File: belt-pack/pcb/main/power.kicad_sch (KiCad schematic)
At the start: 6 parts, among them U2 TP4056

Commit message: Nearly finished with battery circuitry
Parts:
- added C1: 100nF, PCM_JLCPCB:C_0402, symbol PCM_JLCPCB-Capacitors:0402,100nF
- added C2, C3: 10uF, PCM_JLCPCB:C_0603, symbol PCM_JLCPCB-Capacitors:0603,10uF
- added D1: Red, PCM_JLCPCB:D_0603, symbol PCM_JLCPCB-Diodes:LED,0603,Red
- added D2: Green, PCM_JLCPCB:D_0805, symbol PCM_JLCPCB-Diodes:LED,0805,Green
- added R3: 100Ω, PCM_JLCPCB:R_0402, symbol PCM_JLCPCB-Resistors:0402,100Ω
- added R4, R5: 1kΩ, PCM_JLCPCB:R_0402, symbol PCM_JLCPCB-Resistors:0402,1kΩ
- added R6: 1Ω, PCM_JLCPCB:R_1206, symbol PCM_JLCPCB-Resistors:1206,1Ω
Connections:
- net GND: now also R2.2, C2.2, C3.2; no longer U2.6 (STDBY#), U2.7 (CHRG#)
- net USB_5V: now also R6.1; no longer U2.4 (VCC), U2.8 (CE)
- net at BT1.2 (-), Q1.1 (S1): now also C1.2
- net at Q1.6 (G1): now also U3.3 (OC)
- net at U2.5 (BAT): now also BT1.1 (+), C2.1, R3.1; no longer U3.5 (VCC)
- new net: C3.1, R4.1, R5.1, R6.2, U2.4 (VCC), U2.8 (CE)
- new net: D2.2, R5.2
- new net: C1.1, R3.2, U3.5 (VCC)
- new net: D1.2, R4.2
- new net: D2.1, U2.6 (STDBY#)
- new net: D1.1, U2.7 (CHRG#)
- no-connect marks 0 -> 1
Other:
- moved on the sheet: BT1, Q1, R1, R2, U2, U3

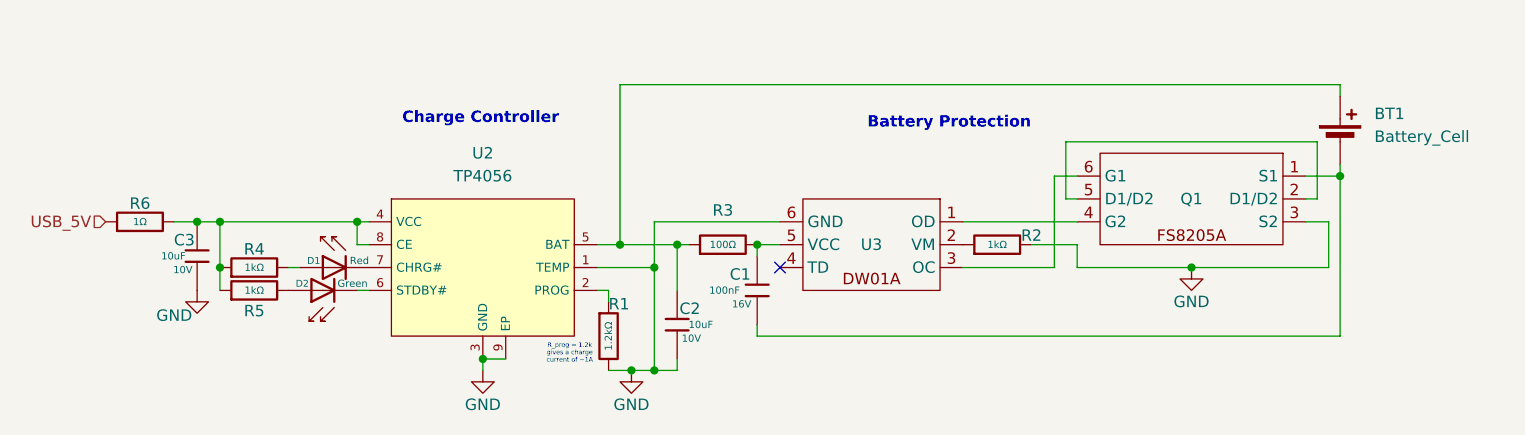
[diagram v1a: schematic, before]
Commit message: Schematic progress
battery charge circuit
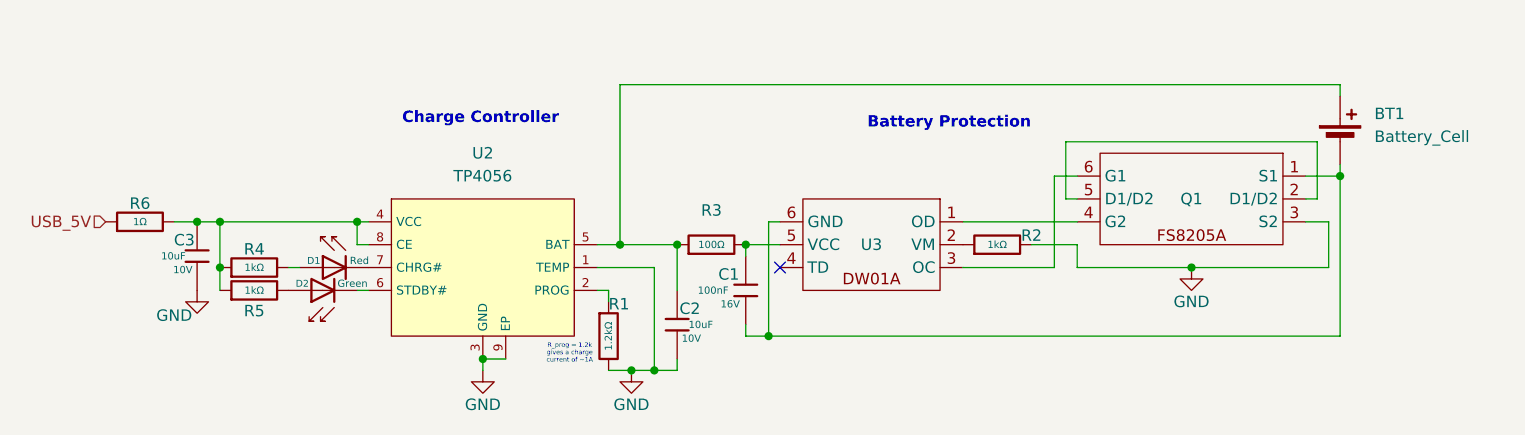
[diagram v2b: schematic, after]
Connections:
- net GND: no longer U3.6 (GND)
- net at BT1.2 (-), C1.2, Q1.1 (S1): now also U3.6 (GND)
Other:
- moved on the sheet: C1, R3
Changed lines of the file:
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@@
 	)
 	(junction
-		(at 165.1 118.11)
+		(at 156.21 118.11)
 		(diameter 0)
 		(color 0 0 0 0)
@@
 	)
 	(junction
-		(at 156.21 118.11)
-		(diameter 0)
-		(color 0 0 0 0)
-	)
-	(junction
-		(at 153.67 120.65)
+		(at 166.37 128.27)
 		(diameter 0)
 		(color 0 0 0 0)
@@
 	)
 	(junction
+		(at 163.83 118.11)
+		(diameter 0)
+		(color 0 0 0 0)
+	)
+	(junction
 		(at 120.65 115.57)
 		(diameter 0)
@@
 	(wire
 		(pts
+			(xy 166.37 115.57) (xy 166.37 128.27)
+		)
+		(stroke
+			(width 0)
+			(type default)
+		)
+	)
+	(wire
+		(pts
 			(xy 213.36 120.65) (xy 228.6 120.65)
 		)
@@
 	(wire
 		(pts
-			(xy 149.86 118.11) (xy 156.21 118.11)
+			(xy 166.37 128.27) (xy 229.87 128.27)
 		)
 		(stroke
@@
 	(wire
 		(pts
-			(xy 156.21 118.11) (xy 157.48 118.11)
+			(xy 149.86 118.11) (xy 156.21 118.11)
 		)
 		(stroke
@@
 	(wire
 		(pts
-			(xy 167.64 115.57) (xy 153.67 115.57)
+			(xy 227.33 106.68) (xy 199.39 106.68)
 		)
 		(stroke
@@
 	(wire
 		(pts
-			(xy 227.33 106.68) (xy 199.39 106.68)
+			(xy 167.64 115.57) (xy 166.37 115.57)
 		)
 		(stroke
@@
 	(wire
 		(pts
-			(xy 165.1 119.38) (xy 165.1 118.11)
+			(xy 163.83 119.38) (xy 163.83 118.11)
 		)
 		(stroke
@@
 	(wire
 		(pts
-			(xy 199.39 113.03) (xy 200.66 113.03)
+			(xy 163.83 118.11) (xy 167.64 118.11)
 		)
 		(stroke
@@
 	(wire
 		(pts
-			(xy 147.32 120.65) (xy 153.67 120.65)
+			(xy 199.39 113.03) (xy 200.66 113.03)
 		)
 		(stroke
@@
 	(wire
 		(pts
-			(xy 120.65 123.19) (xy 121.92 123.19)
+			(xy 147.32 120.65) (xy 153.67 120.65)
 		)
 		(stroke
@@
 	(wire
 		(pts
-			(xy 147.32 118.11) (xy 149.86 118.11)
+			(xy 120.65 123.19) (xy 121.92 123.19)
 		)
 		(stroke
@@
 	(wire
 		(pts
-			(xy 165.1 128.27) (xy 229.87 128.27)
+			(xy 147.32 118.11) (xy 149.86 118.11)
 		)
 		(stroke
@@
 	(wire
 		(pts
-			(xy 229.87 100.33) (xy 149.86 100.33)
+			(xy 163.83 128.27) (xy 166.37 128.27)
 		)
 		(stroke
@@
 	(wire
 		(pts
-			(xy 187.96 120.65) (xy 198.12 120.65)
+			(xy 229.87 100.33) (xy 149.86 100.33)
 		)
 		(stroke
@@
 	(wire
 		(pts
-			(xy 199.39 106.68) (xy 199.39 113.03)
+			(xy 187.96 120.65) (xy 198.12 120.65)
 		)
 		(stroke
@@
 	(wire
 		(pts
-			(xy 153.67 115.57) (xy 153.67 120.65)
+			(xy 199.39 106.68) (xy 199.39 113.03)
 		)
 		(stroke
@@
 	(wire
 		(pts
-			(xy 165.1 128.27) (xy 165.1 127)
+			(xy 163.83 128.27) (xy 163.83 127)
 		)
 		(stroke
@@
 	(wire
 		(pts
-			(xy 165.1 118.11) (xy 167.64 118.11)
-		)
-		(stroke
-			(width 0)
-			(type default)
-		)
-	)
-	(wire
-		(pts
 			(xy 102.87 115.57) (xy 105.41 115.57)
 		)
@@
 	(symbol
 		(lib_id "PCM_JLCPCB-Resistors:0402,100Ω")
-		(at 161.29 118.11 90)
+		(at 160.02 118.11 90)
 		(unit 1)
 		(body_style 1)
@@
 		(fields_autoplaced yes)
 		(property "Reference" "R3"
-			(at 161.29 114.3 90)
+			(at 160.02 114.3 90)
 			(show_name no)
 			(do_not_autoplace no)
@@
 		)
 		(property "Value" "100Ω"
-			(at 161.29 118.11 90)
+			(at 160.02 118.11 90)
 			(show_name no)
 			(do_not_autoplace yes)
@@
 		)
 		(property "Footprint" "PCM_JLCPCB:R_0402"
-			(at 161.29 119.888 90)
+			(at 160.02 119.888 90)
 			(hide yes)
 			(show_name no)
@@
 		)
 		(property "Datasheet" "https://www.lcsc.com/datasheet/lcsc_datasheet_2205311900_UNI-ROYAL-Uniroyal-Elec-0402WGF1000TCE_C25076.pdf"
-			(at 161.29 118.11 0)
+			(at 160.02 118.11 0)
 			(hide yes)
 			(show_name no)
@@
 		)
 		(property "Description" "62.5mW Thick Film Resistors 50V ±1% ±200ppm/°C 100Ω 0402 Chip Resistor - Surface Mount ROHS"
-			(at 161.29 118.11 0)
+			(at 160.02 118.11 0)
 			(hide yes)
 			(show_name no)
@@
 		)
 		(property "LCSC" "C25076"
-			(at 161.29 118.11 0)
+			(at 160.02 118.11 0)
 			(hide yes)
 			(show_name no)
@@
 		)
 		(property "Stock" "5907585"
-			(at 161.29 118.11 0)
+			(at 160.02 118.11 0)
 			(hide yes)
 			(show_name no)
@@
 		)
 		(property "Price" "0.004USD"
-			(at 161.29 118.11 0)
+			(at 160.02 118.11 0)
 			(hide yes)
 			(show_name no)
@@
 		)
 		(property "Process" "SMT"
-			(at 161.29 118.11 0)
+			(at 160.02 118.11 0)
 			(hide yes)
 			(show_name no)
@@
 		)
 		(property "Minimum Qty" "20"
-			(at 161.29 118.11 0)
+			(at 160.02 118.11 0)
 			(hide yes)
 			(show_name no)
@@
 		)
 		(property "Attrition Qty" "10"
-			(at 161.29 118.11 0)
+			(at 160.02 118.11 0)
 			(hide yes)
 			(show_name no)
@@
 		)
 		(property "Class" "Basic Component"
-			(at 161.29 118.11 0)
+			(at 160.02 118.11 0)
 			(hide yes)
 			(show_name no)
@@
 		)
 		(property "Category" "Resistors,Chip Resistor - Surface Mount"
-			(at 161.29 118.11 0)
+			(at 160.02 118.11 0)
 			(hide yes)
 			(show_name no)
@@
 		)
 		(property "Manufacturer" "UNI-ROYAL(Uniroyal Elec)"
-			(at 161.29 118.11 0)
+			(at 160.02 118.11 0)
 			(hide yes)
 			(show_name no)
@@
 		)
 		(property "Part" "0402WGF1000TCE"
-			(at 161.29 118.11 0)
+			(at 160.02 118.11 0)
 			(hide yes)
 			(show_name no)
@@
 		)
 		(property "Resistance" "100Ω"
-			(at 161.29 118.11 0)
+			(at 160.02 118.11 0)
 			(hide yes)
 			(show_name no)
@@
 		)
 		(property "Power(Watts)" "62.5mW"
-			(at 161.29 118.11 0)
+			(at 160.02 118.11 0)
 			(hide yes)
 			(show_name no)
@@
 		)
 		(property "Type" "Thick Film Resistors"
-			(at 161.29 118.11 0)
+			(at 160.02 118.11 0)
 			(hide yes)
 			(show_name no)
@@
 		)
 		(property "Overload Voltage (Max)" "50V"
-			(at 161.29 118.11 0)
+			(at 160.02 118.11 0)
 			(hide yes)
 			(show_name no)
@@
 		)
 		(property "Operating Temperature Range" "-55°C~+155°C"
-			(at 161.29 118.11 0)
+			(at 160.02 118.11 0)
 			(hide yes)
 			(show_name no)
@@
 		)
 		(property "Tolerance" "±1%"
-			(at 161.29 118.11 0)
+			(at 160.02 118.11 0)
 			(hide yes)
 			(show_name no)
@@
 		)
 		(property "Temperature Coefficient" "±200ppm/°C"
-			(at 161.29 118.11 0)
+			(at 160.02 118.11 0)
 			(hide yes)
 			(show_name no)
@@
 	(symbol
 		(lib_id "PCM_JLCPCB-Capacitors:0402,100nF")
-		(at 165.1 123.19 0)
+		(at 163.83 123.19 0)
 		(unit 1)
 		(body_style 1)
@@
 		(dnp no)
 		(property "Reference" "C1"
-			(at 162.052 121.412 0)
+			(at 160.782 121.412 0)
 			(show_name no)
 			(do_not_autoplace no)
@@
 		)
 		(property "Value" "100nF"
-			(at 159.766 123.19 0)
+			(at 158.496 123.19 0)
 			(show_name no)
 			(do_not_autoplace no)
@@
 		)
 		(property "Footprint" "PCM_JLCPCB:C_0402"
-			(at 163.322 123.19 90)
+			(at 162.052 123.19 90)
 			(hide yes)
 			(show_name no)
@@
 		)
 		(property "Datasheet" "https://www.lcsc.com/datasheet/lcsc_datasheet_2304140030_Samsung-Electro-Mechanics-CL05B104KO5NNNC_C1525.pdf"
-			(at 165.1 123.19 0)
+			(at 163.83 123.19 0)
 			(hide yes)
 			(show_name no)
@@
 		)
 		(property "Description" "16V 100nF X7R ±10% 0402 Multilayer Ceramic Capacitors MLCC - SMD/SMT ROHS"
-			(at 165.1 123.19 0)
+			(at 163.83 123.19 0)
 			(hide yes)
 			(show_name no)
@@
 		)
 		(property "LCSC" "C1525"
-			(at 165.1 123.19 0)
+			(at 163.83 123.19 0)
 			(hide yes)
 			(show_name no)
@@
 		)
 		(property "Stock" "20208285"
-			(at 165.1 123.19 0)
+			(at 163.83 123.19 0)
 			(hide yes)
 			(show_name no)
@@
 		)
 		(property "Price" "0.004USD"
-			(at 165.1 123.19 0)
+			(at 163.83 123.19 0)
 			(hide yes)
 			(show_name no)
@@
 		)
 		(property "Process" "SMT"
-			(at 165.1 123.19 0)
+			(at 163.83 123.19 0)
 			(hide yes)
 			(show_name no)
@@
 		)
 		(property "Minimum Qty" "20"
-			(at 165.1 123.19 0)
+			(at 163.83 123.19 0)
 			(hide yes)
 			(show_name no)
@@
 		)
 		(property "Attrition Qty" "10"
-			(at 165.1 123.19 0)
+			(at 163.83 123.19 0)
 			(hide yes)
 			(show_name no)
@@
 		)
 		(property "Class" "Basic Component"
-			(at 165.1 123.19 0)
+			(at 163.83 123.19 0)
 			(hide yes)
 			(show_name no)
@@
 		)
 		(property "Category" "Capacitors,Multilayer Ceramic Capacitors MLCC - SMD/SMT"
-			(at 165.1 123.19 0)
+			(at 163.83 123.19 0)
 			(hide yes)
 			(show_name no)
@@
 		)
 		(property "Manufacturer" "Samsung Electro-Mechanics"
-			(at 165.1 123.19 0)
+			(at 163.83 123.19 0)
 			(hide yes)
 			(show_name no)
@@
 		)
 		(property "Part" "CL05B104KO5NNNC"
-			(at 165.1 123.19 0)
+			(at 163.83 123.19 0)
 			(hide yes)
 			(show_name no)
@@
 		)
 		(property "Voltage Rated" "16V"
-			(at 162.306 124.714 0)
+			(at 161.036 124.714 0)
 			(show_name no)
 			(do_not_autoplace no)
@@
 		)
 		(property "Tolerance" "±10%"
-			(at 165.1 123.19 0)
+			(at 163.83 123.19 0)
 			(hide yes)
 			(show_name no)
@@
 		)
 		(property "Capacitance" "100nF"
-			(at 165.1 123.19 0)
+			(at 163.83 123.19 0)
 			(hide yes)
 			(show_name no)
@@
 		)
 		(property "Temperature Coefficient" "X7R"
-			(at 165.1 123.19 0)
+			(at 163.83 123.19 0)
 			(hide yes)
 			(show_name no)
